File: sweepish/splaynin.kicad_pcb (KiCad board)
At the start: 2 copper layers, 127.3 x 101 mm, 37 parts

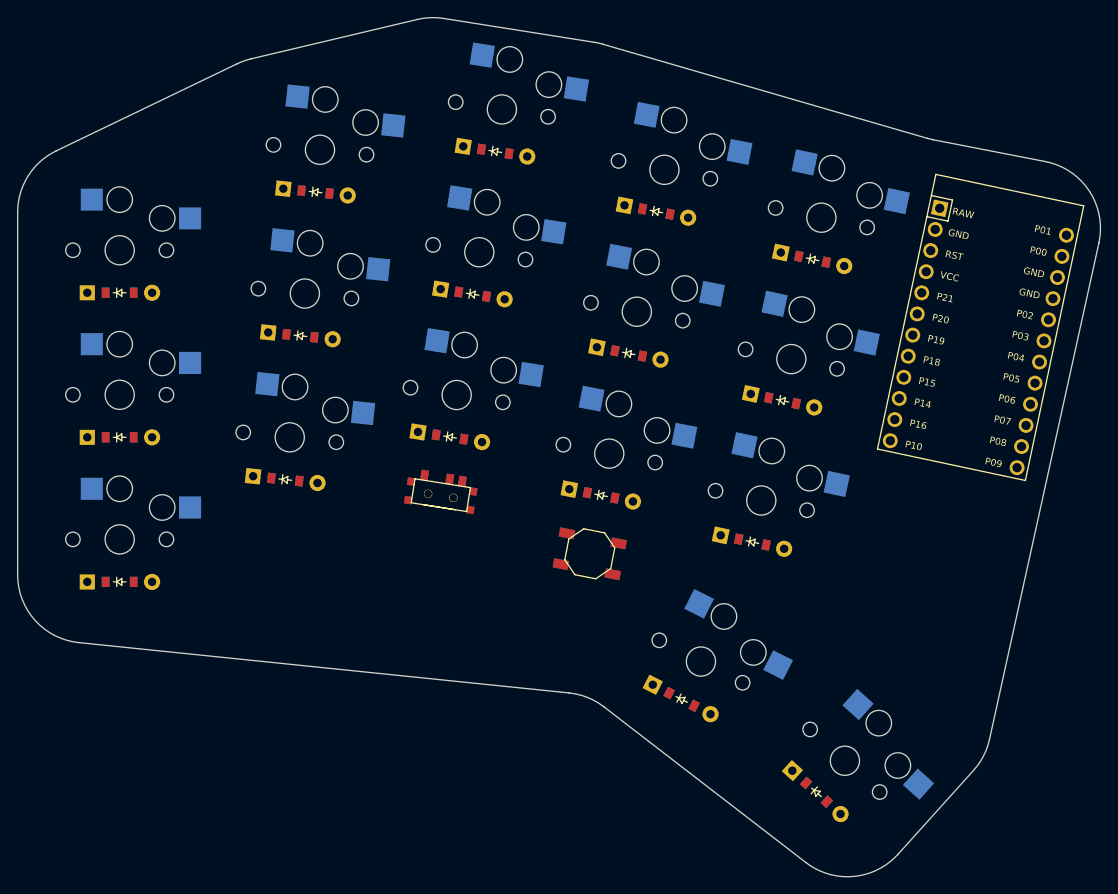
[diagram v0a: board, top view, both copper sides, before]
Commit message: Add xiao cutout footprint to utility board.
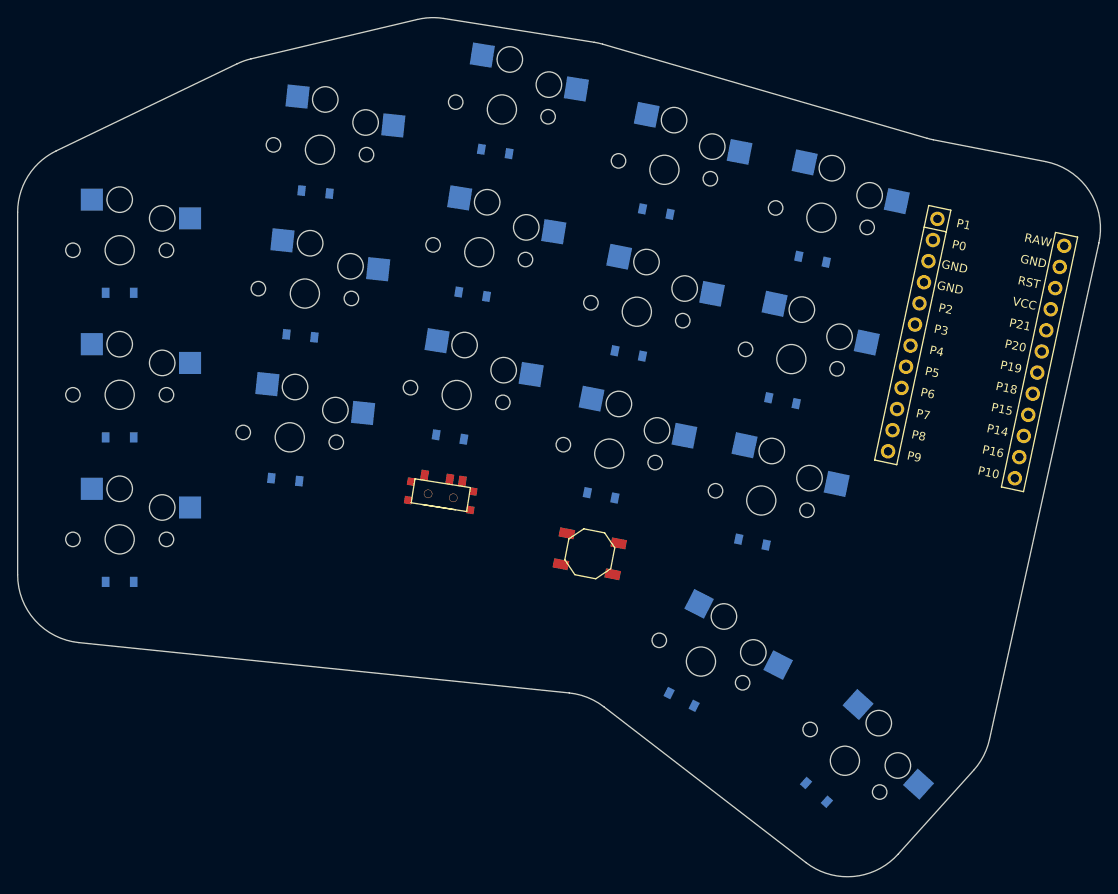
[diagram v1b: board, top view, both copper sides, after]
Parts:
- D1, D10, D11, D12, D13, D14, D15, D16, D17, D2, D3, D4, D5, D6, D7, D8, D9: footprint ComboDiode -> ceoloide:diode_tht_sod123; moved to B.Cu
- MCU1: footprint ProMicro -> ceoloide:mcu_nice_nano
- turned MCU1 to -12 degrees
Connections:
- MCU1 pad 13: P1 -> P9
- MCU1 pad 14: P0 -> P8
- MCU1 pad 15: GND -> P7
- MCU1 pad 16: GND -> P6
- MCU1 pad 17: P2 -> P5
- MCU1 pad 18: P3 -> P4
- MCU1 pad 19: P4 -> P3
- MCU1 pad 20: P5 -> P2
- MCU1 pad 21: P6 -> GND
- MCU1 pad 22: P7 -> GND
- MCU1 pad 23: P8 -> P0
- MCU1 pad 24: P9 -> P1
